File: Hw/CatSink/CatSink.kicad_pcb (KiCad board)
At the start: 2 copper layers, 45 x 20 mm, 36 parts, among them J1 Vout, P1 USB_C_Plug_USB2.0, Q1 SI3421DV, Q2 SI3421DV, SW1 Voltage, SW2 Curent, U1 CYPD3177-24LQXI

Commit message: fix pcb
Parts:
- moved J1 0.78 mm to (158.9, 100.0)
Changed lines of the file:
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@@
   )
   (module TerminalBlock:TerminalBlock_bornier-2_P5.08mm (layer F.Cu)
-    (at 158.95 99.225 270)
+    (at 158.95 100 270)
     (descr "simple 2-pin terminal block, pitch 5.08mm, revamped version of bornier2")
     (tags "terminal block bornier2")
@@
     (tags capacitor)
     (attr smd)
-    (fp_text reference C10 (at -3.72 0.04) (layer F.SilkS)
+    (fp_text reference C10 (at -3.225 0.675) (layer F.SilkS)
       (effects (font (size 0.6 0.6) (thickness 0.1)))
     )
@@
     )
   )
-  (gr_line (start 163 93) (end 118 93) (layer Edge.Cuts) (width 0.05))
-  (gr_line (start 163 113) (end 163 93) (layer Edge.Cuts) (width 0.05))
-  (gr_line (start 118 113) (end 163 113) (layer Edge.Cuts) (width 0.05))
-  (gr_line (start 118 93) (end 118 113) (layer Edge.Cuts) (width 0.05))
+  (gr_line (start 163 92.5) (end 118 92.5) (layer Edge.Cuts) (width 0.05))
+  (gr_line (start 163 112.5) (end 163 92.5) (layer Edge.Cuts) (width 0.05))
+  (gr_line (start 118 112.5) (end 163 112.5) (layer Edge.Cuts) (width 0.05))
+  (gr_line (start 118 92.5) (end 118 112.5) (layer Edge.Cuts) (width 0.05))
   (dimension 45 (width 0.12) (layer Margin)
     (gr_text "45,000 mm" (at 140.5 136.27) (layer Margin)

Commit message: added logos
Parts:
- added G***: LOGO, Aesthetics:electronic_cats_logo_8x6, B.Cu at (131.1, 102.6)
- added G***: LOGO, Aesthetics:electronic_cats_logo_4x3, F.Cu at (158.0, 109.6)
- added REF**: OSHW-Logo_5.7x6mm_SilkScreen, Symbol:OSHW-Logo_5.7x6mm_SilkScreen, B.Cu at (149.6, 102.6)

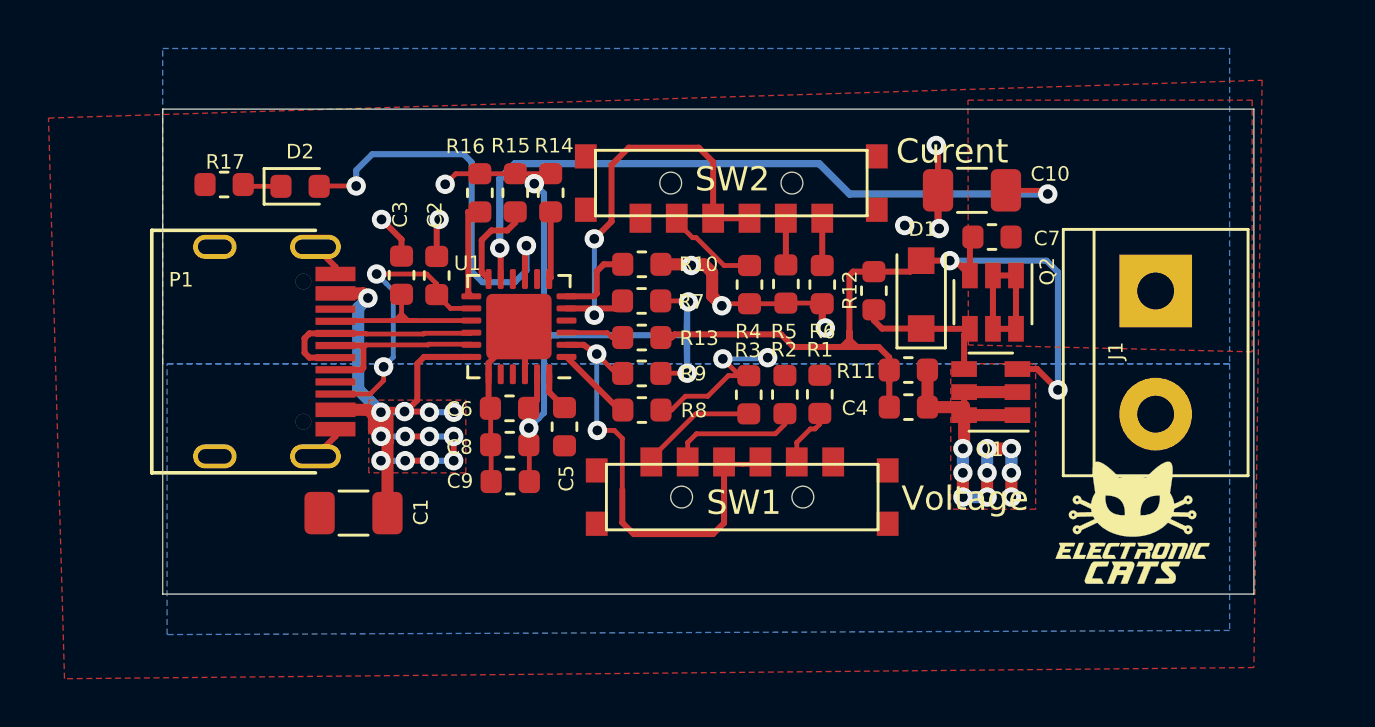
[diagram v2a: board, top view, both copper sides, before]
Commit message: Added Led and 3D switch
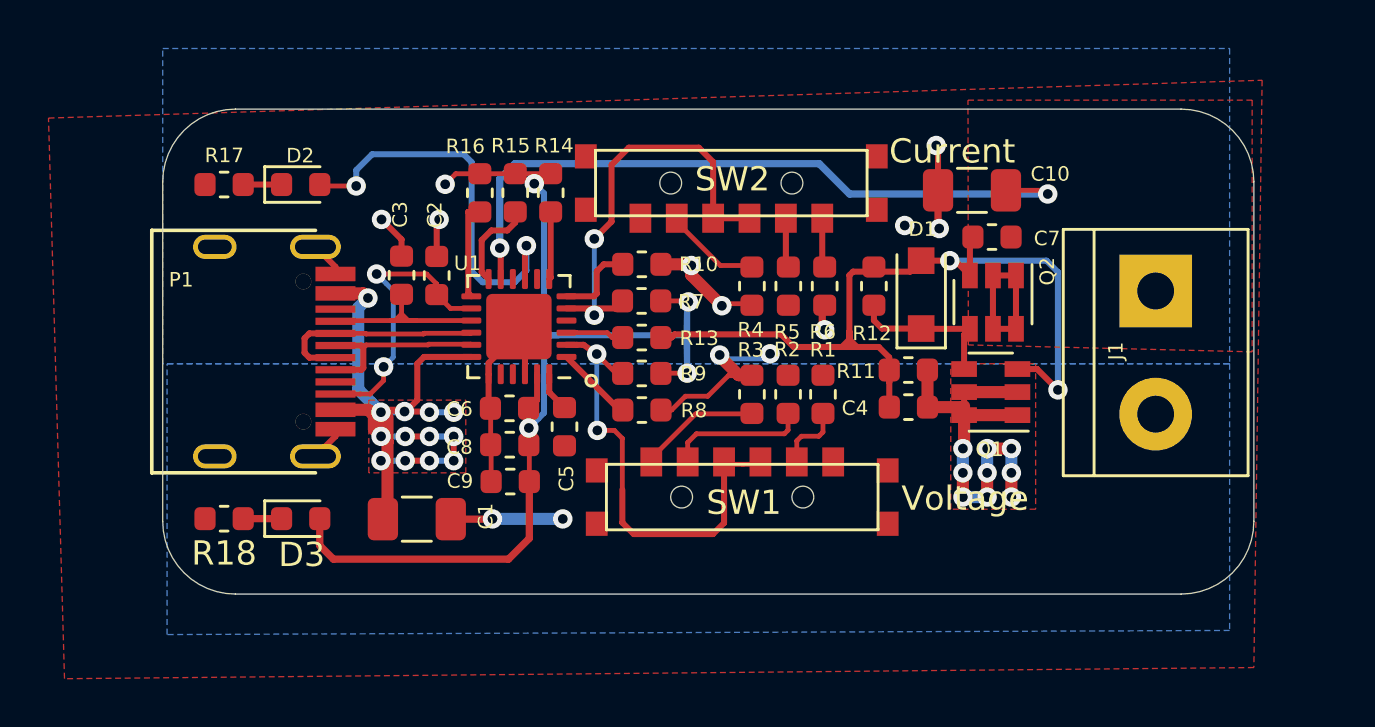
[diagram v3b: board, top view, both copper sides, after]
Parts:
- removed G***: LOGO, Aesthetics:electronic_cats_logo_8x6
- removed G***: LOGO, Aesthetics:electronic_cats_logo_4x3
- removed REF**: OSHW-Logo_5.7x6mm_SilkScreen, Symbol:OSHW-Logo_5.7x6mm_SilkScreen
- added D3: Power, LED_SMD:LED_0603_1608Metric, F.Cu at (123.7, 109.4)
- added R18: 1K, Resistor_SMD:R_0603_1608Metric, F.Cu at (120.5, 109.4)
- R11: value 1K -> 10K
- SW2: value Curent -> Current
- moved C1 2.62 mm to (128.5, 109.4), turned to 0 degrees
- moved R12 0.19 mm to (147.3, 99.8)
- moved R5 0.13 mm to (143.8, 99.8)
- moved R3 0.13 mm to (142.3, 104.3)
- moved R2 0.13 mm to (143.8, 104.3)
- moved R1 0.13 mm to (145.2, 104.3)
- moved R4 0.12 mm to (142.3, 99.8)
- moved R6 0.12 mm to (145.3, 99.8)
- moved D2 0.08 mm to (123.7, 95.6)
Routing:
- net +3V3: track 35.9 -> 48.7 mm
- net Net-(D3-Pad1): track 0.00 -> 1.58 mm
- net GND: track 36.7 -> 37.9 mm, vias 10 -> 12
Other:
- outline, holes or cut-outs redrawn

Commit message: fix traces
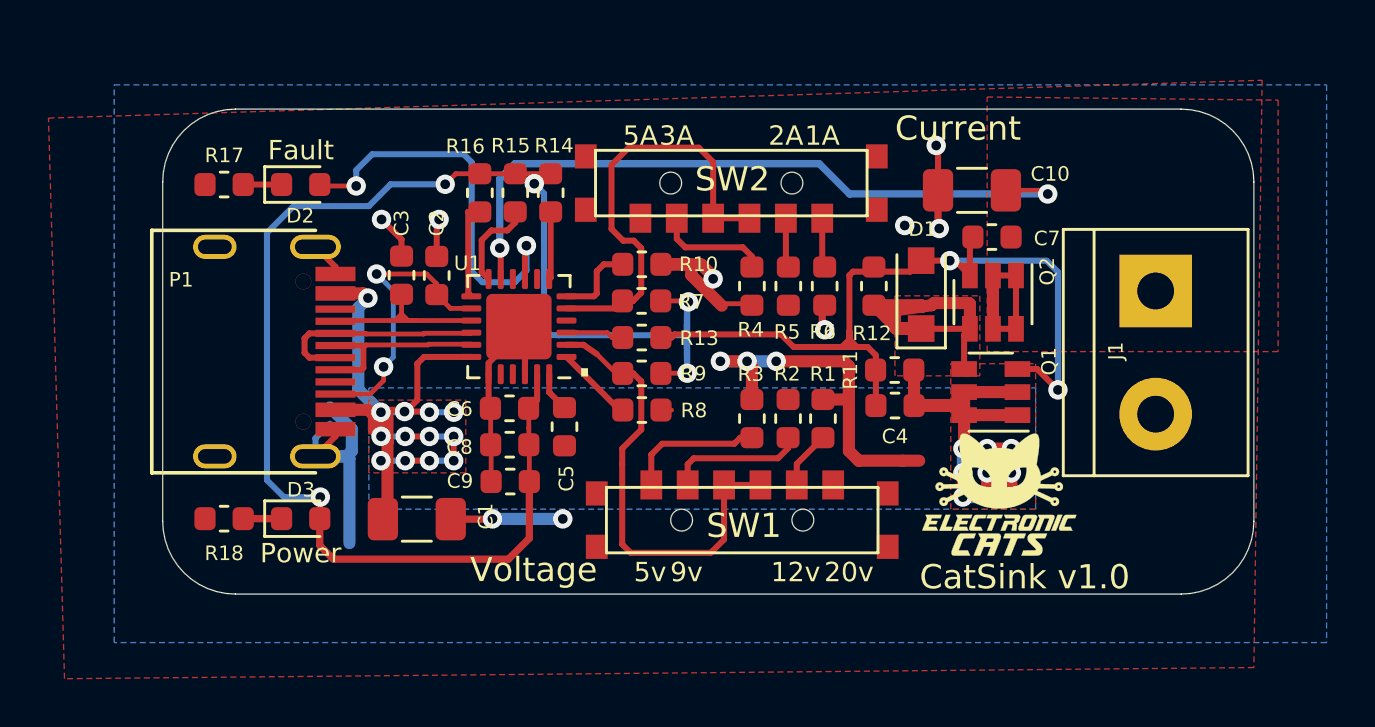
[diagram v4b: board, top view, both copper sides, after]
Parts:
- added G***: LOGO, Aesthetics:electronic_cats_logo_4x3, B.Cu at (131.2, 102.5)
- added G***: LOGO, Aesthetics:electronic_cats_logo_4x3, F.Cu at (152.5, 108.4)
- added REF**: OSHW-Logo2_7.3x6mm_SilkScreen, Symbol:OSHW-Logo2_7.3x6mm_SilkScreen, B.Cu at (150.9, 102.1)
- moved R1 1.00 mm to (145.2, 105.3)
- moved R2 1.00 mm to (143.8, 105.3)
- moved R3 1.00 mm to (142.3, 105.3)
- moved SW1 0.95 mm to (141.9, 109.5)
- moved R11 0.56 mm to (148.2, 103.3)
- moved C4 0.56 mm to (148.2, 104.7)
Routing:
- net GND: track 37.9 -> 59.1 mm
- net +3V3: track 48.7 -> 64.8 mm
- net Net-(D1-Pad1): track 6.30 -> 15.0 mm
- net VBUS: track 55.2 -> 58.9 mm
- net /Icoarse: track 18.7 -> 17.9 mm, vias 2 -> 0
- net /3A: track 3.90 -> 4.69 mm
- net /5v: track 4.93 -> 5.69 mm
- net Net-(C4-Pad2): track 34.7 -> 34.2 mm
- net /Vmax: track 19.3 -> 19.0 mm, vias 2 -> 0
- added copper zone on F.Cu, net Net-(D1-Pad1)
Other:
- board text added: "."
- board text added: "12v"
- board text added: "1A"
- board text added: "20v"
- board text added: "2A"
- board text added: "3A"
- board text added: "5A"
- board text added: "5v"
- board text added: "9v"
- board text added: "CatSink v1.0"

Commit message: fix (hw): change notations from margin to user drawings
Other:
- net class Default removed
- net class vcc removed
